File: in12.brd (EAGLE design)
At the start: 146.1 x 43.2 mm, 34 parts, among them U1 MICROCHIP_HV5622PG-GMICROCHIP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, U2 MICROCHIP_HV5622PG-GMICROCHIP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, U3 MICROCHIP_HV5622PG-GMICROCHIP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

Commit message: 5523 still need shuffle pins
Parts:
- removed U1, U2, U3: MICROCHIP_HV5622PG-GMICROCHIP_HV5622PG-G_0_0, Microchip - HV5622PG-G:MICROCHIP_HV5622PG-G_0
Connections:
- net L10: no longer U1.35
- net L11: no longer U1.40
- net L12: no longer U1.44
- net L13: no longer U1.43
- net L14: no longer U1.42
- net L15: no longer U1.41
- net L16: no longer U1.39
- net L17: no longer U1.37
- net L18: no longer U1.36
- net L19: no longer U1.38
- net L1D: no longer U1.1
- net L20: no longer U1.2
- net L21: no longer U1.7
- net L22: no longer U1.11
- net L23: no longer U1.10
- net L24: no longer U1.9
- net L25: no longer U1.8
- net L26: no longer U1.6
- net L27: no longer U1.4
- net L28: no longer U1.3
- net L29: no longer U1.5
- net L2D: no longer U1.22
- net L30: no longer U1.12
- net L31: no longer U1.17
- net L32: no longer U1.21
- net L33: no longer U1.20
- net L34: no longer U1.19
- net L35: no longer U1.18
- net L36: no longer U1.16
- net L37: no longer U1.14
- net L38: no longer U1.13
- net L39: no longer U1.15
- net L3D: now also U5.35; no longer U2.35
- net L40: now also U5.36; no longer U2.36
- net L41: now also U5.41; no longer U2.41
- net L42: now also U5.4; no longer U2.4
- net L43: now also U5.2; no longer U2.2
- net L44: now also U5.43; no longer U2.43
- net L45: now also U5.42; no longer U2.42
- net L46: now also U5.40; no longer U2.40
- net L47: now also U5.38; no longer U2.38
- net L48: now also U5.37; no longer U2.37
- net L49: now also U5.39; no longer U2.39
- net L4D: now also U5.5; no longer U2.5
- net L50: now also U5.7; no longer U2.7
- net L51: now also U5.13; no longer U2.13
- net L52: now also U5.17; no longer U2.17
- net L53: now also U5.16; no longer U2.16
- net L54: now also U5.15; no longer U2.15
- net L55: now also U5.14; no longer U2.14
- net L56: now also U5.12; no longer U2.12
- net L57: now also U5.10; no longer U2.10
- net L58: now also U5.8; no longer U2.8
- net L59: now also U5.11; no longer U2.11
- net L5D: now also U5.18; no longer U2.18
- net L60: now also U5.19; no longer U2.19
- net L61: now also U6.36; no longer U3.36
- net L62: now also U6.43; no longer U3.43
- net L63: now also U6.42; no longer U3.42
- net L64: now also U6.38; no longer U3.38
- net L65: now also U6.37; no longer U3.37
- net L66: now also U6.35; no longer U3.35
- net L67: now also U5.22; no longer U2.22
- net L68: now also U5.21; no longer U2.21
- net L69: now also U5.20; no longer U2.20
- net L6D: now also U6.44; no longer U3.44
- net L70: now also U6.1; no longer U3.1
- net L71: now also U6.6; no longer U3.6
- net L72: now also U6.10; no longer U3.10
- net L73: now also U6.9; no longer U3.9
- net L74: now also U6.8; no longer U3.8
- net L75: now also U6.7; no longer U3.7
- net L76: now also U6.5; no longer U3.5
- net L77: now also U6.3; no longer U3.3
- net L78: now also U6.2; no longer U3.2
- net L79: now also U6.4; no longer U3.4
- net L7D: now also U6.11; no longer U3.11
- net L80: now also U6.12; no longer U3.12
- net L81: now also U6.17; no longer U3.17
- net L82: now also U6.21; no longer U3.21
- net L83: now also U6.20; no longer U3.20
- net L84: now also U6.19; no longer U3.19
- net L85: now also U6.18; no longer U3.18
- net L86: now also U6.16; no longer U3.16
- net L87: now also U6.14; no longer U3.14
- net L88: now also U6.13; no longer U3.13
- net L89: now also U6.15; no longer U3.15
- net L8D: now also U6.22; no longer U3.22
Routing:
- net L10: track 57.2 -> 13.2 mm
- net L8D: track 72.8 -> 30.7 mm
- net L82: track 58.2 -> 17.1 mm
- net L83: track 50.4 -> 10.8 mm
- net L18: track 43.3 -> 4.93 mm
- net L84: track 43.0 -> 6.01 mm
- net L17: track 36.9 -> 2.40 mm
- net L85: track 37.5 -> 3.11 mm
- net L81: track 51.6 -> 20.0 mm
- net L19: track 42.8 -> 12.2 mm
- net L86: track 31.0 -> 2.74 mm
- net L16: track 29.6 -> 2.93 mm
- net L51: track 26.5 -> 0.00 mm
- net L89: track 39.4 -> 13.0 mm
- net L3D: track 39.0 -> 14.3 mm
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
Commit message: hv single layer routed
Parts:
- added U$1: DS3232, ds3232:SO20-2
- moved R1 9.58 mm to (2.29, 8.00), turned to 270 degrees
- moved R16 9.27 mm to (144.1, 8.64), turned to 90 degrees
- moved R7 4.76 mm to (110.4, 7.75)
- moved R6 4.68 mm to (92.2, 7.37)
- moved R5 4.60 mm to (74.5, 7.37)
- moved R8 4.47 mm to (128.3, 7.49)
- moved R2 4.42 mm to (21.3, 7.24)
- moved R3 4.42 mm to (39.1, 7.24)
- moved R4 4.37 mm to (57.1, 7.37)
- moved U4 2.18 mm to (36.8, 30.0)
- moved U6 1.99 mm to (108.8, 30.0)
- moved U5 1.37 mm to (72.4, 30.0), turned to 135 degrees
- moved R9 1.25 mm to (17.9, 7.11)
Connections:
- net L2D: now also U4.12; no longer U4.22
- net L30: now also U4.13; no longer U4.12
- net L31: now also U4.18; no longer U4.17
- net L32: now also U4.22; no longer U4.21
- net L33: now also U4.21; no longer U4.20
- net L34: now also U4.20; no longer U4.19
- net L35: now also U4.19; no longer U4.18
- net L36: now also U4.17; no longer U4.16
- net L37: now also U4.15; no longer U4.14
- net L38: now also U4.14; no longer U4.13
- net L39: now also U4.16; no longer U4.15
- net L41: now also U5.42; no longer U5.41
- net L42: now also U5.1; no longer U5.4
- net L43: now also U5.44; no longer U5.2
- net L45: now also U5.41; no longer U5.42
- net L4D: now also U5.2; no longer U5.5
- net L50: now also U5.3; no longer U5.7
- net L51: now also U5.8; no longer U5.13
- net L52: now also U5.12; no longer U5.17
- net L53: now also U5.11; no longer U5.16
- net L54: now also U5.10; no longer U5.15
- net L55: now also U5.9; no longer U5.14
- net L56: now also U5.7; no longer U5.12
- net L57: now also U5.5; no longer U5.10
- net L58: now also U5.4; no longer U5.8
- net L59: now also U5.6; no longer U5.11
- net L5D: now also U5.13; no longer U5.18
- net L60: now also U5.14; no longer U5.19
- net L61: now also U6.39; no longer U6.36
- net L64: now also U6.41; no longer U6.38
- net L65: now also U6.40; no longer U6.37
- net L66: now also U6.38; no longer U6.35
- net L67: now also U6.37; no longer U5.22
- net L68: now also U6.36; no longer U5.21
- net L69: now also U6.35; no longer U5.20
- net L71: now also U6.5; no longer U6.6
- net L76: now also U6.6; no longer U6.5
- net L77: now also U6.4; no longer U6.3
- net L79: now also U6.3; no longer U6.4
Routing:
- net HV: track 119.3 -> 0.00 mm
- net VDD: track 0.00 -> 77.7 mm
- net L10: track 13.2 -> 52.1 mm
- net L82: track 17.1 -> 53.9 mm
- net L83: track 10.8 -> 47.0 mm
- net L18: track 4.93 -> 40.6 mm
- net L84: track 6.01 -> 39.8 mm
- net L17: track 2.40 -> 34.2 mm
- net L85: track 3.11 -> 34.5 mm
- net L19: track 12.2 -> 41.1 mm
- net L81: track 20.0 -> 48.7 mm
- net L51: track 0.00 -> 27.3 mm
- net L86: track 2.74 -> 28.3 mm
- net L8D: track 30.7 -> 55.7 mm
- net L16: track 2.93 -> 27.7 mm
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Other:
- board size 146.1 x 43.2 mm -> 146.1 x 38.1 mm

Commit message: compact
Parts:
- added IC1: LM1117MPX-3.3_NOPB, SamacSys_Parts:SOT230P700X180-4N
- added U$2: HV_PSU, SamacSys_Parts:HV_PSU
- added U1: ESP32-WROOM-32D, SamacSys_Parts:MODULE_ESP32-WROOM-32D
- moved R16 9.67 mm to (134.5, 8.13), turned to 0 degrees
- moved SV1 9.67 mm to (12.2, 56.6)
- moved R13 8.65 mm to (81.5, 8.13), turned to 0 degrees
- moved R10 8.64 mm to (28.2, 8.00), turned to 0 degrees
- moved R14 8.52 mm to (99.4, 8.13), turned to 0 degrees
- moved R11 8.52 mm to (46.1, 8.00), turned to 0 degrees
- moved R12 8.52 mm to (63.9, 8.00), turned to 0 degrees
- moved R15 8.51 mm to (117.2, 7.75), turned to 0 degrees
- moved R9 7.42 mm to (10.5, 8.00), turned to 0 degrees
- moved R1 4.19 mm to (2.41, 3.81)
- moved R7 4.14 mm to (109.1, 3.81)
- moved R8 3.94 mm to (126.9, 3.81)
- moved R4 3.82 mm to (55.8, 3.81)
- moved R5 3.70 mm to (73.5, 3.81)
- moved R6 3.67 mm to (91.3, 3.81)
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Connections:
- new net 3V3: U1.2
- new net GND: U1.1, U1.15, U1.38, U1.39_1, U1.39_10, U1.39_11, U1.39_12, U1.39_13, U1.39_14, U1.39_15, U1.39_16, U1.39_17, U1.39_18, U1.39_19, U1.39_2, U1.39_20, U1.39_21, U1.39_3, U1.39_4, U1.39_5, U1.39_6, U1.39_7, U1.39_8, U1.39_9
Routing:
- net HV: track 0.00 -> 144.4 mm
- net L8D: track 55.7 -> 68.7 mm
- net L2D: track 17.5 -> 29.3 mm
- net L5D: track 34.8 -> 46.5 mm
- net L6D: track 17.6 -> 29.1 mm
- net L3D: track 33.9 -> 45.1 mm
- net L4D: track 18.6 -> 29.9 mm
- net L1D: track 32.4 -> 42.8 mm
- net L7D: track 33.2 -> 42.5 mm
- net N$15: track 10.0 -> 3.98 mm
- net N$11: track 10.0 -> 4.23 mm
- net N$12: track 10.0 -> 4.23 mm
- net N$10: track 10.0 -> 4.28 mm
- net N$14: track 10.0 -> 4.36 mm
- net N$13: track 10.0 -> 4.41 mm
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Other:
- board size 146.1 x 38.1 mm -> 146.1 x 33.7 mm

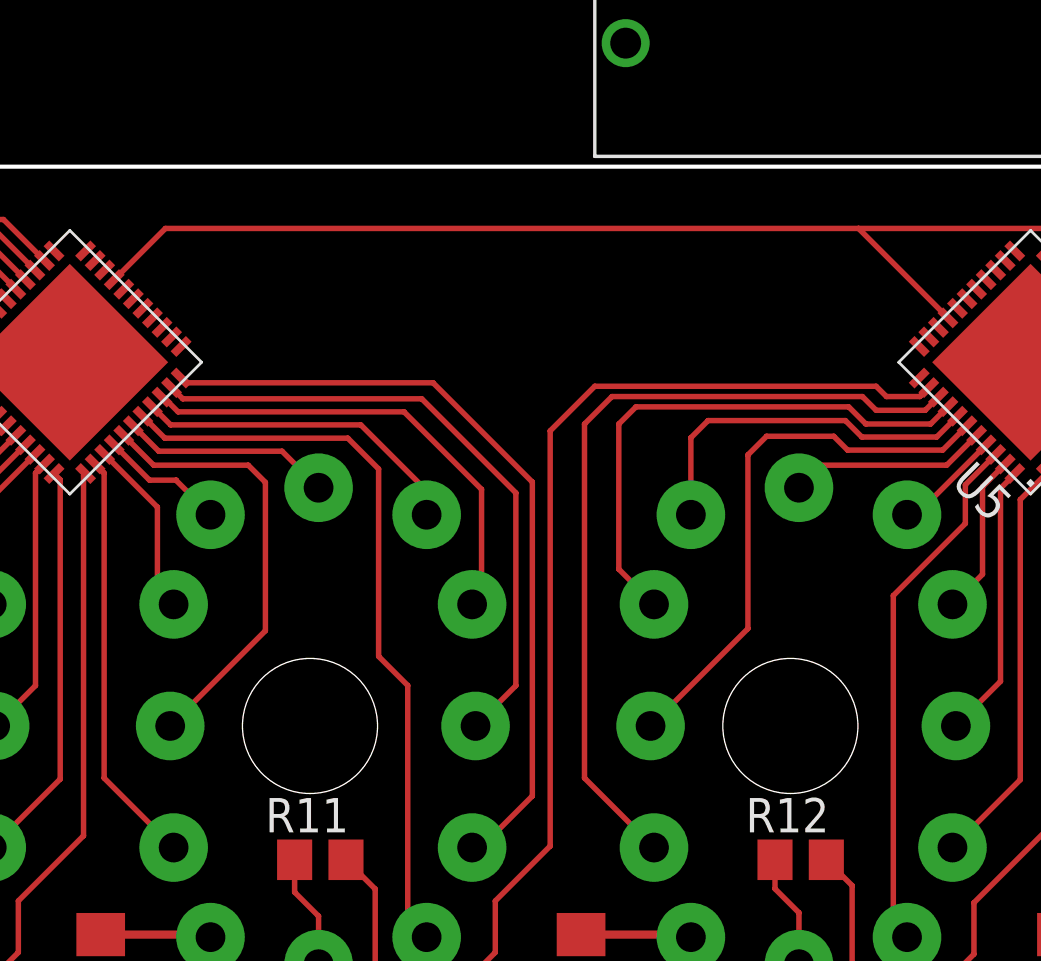
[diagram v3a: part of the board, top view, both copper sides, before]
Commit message: added m.2 connector
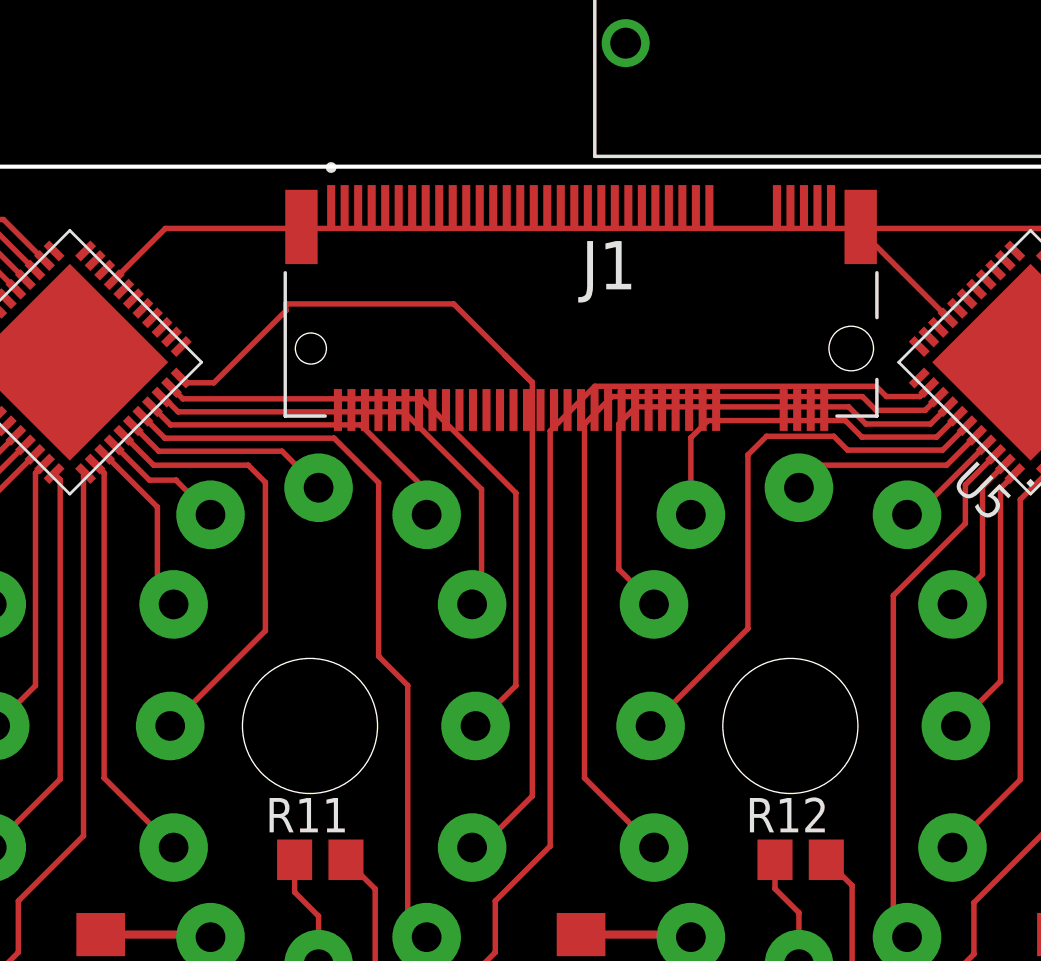
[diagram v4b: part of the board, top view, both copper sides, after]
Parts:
- added J1: 1-2199230-6, 1-2199230-6:TE_1-2199230-6
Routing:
- net L32: track 29.2 -> 35.4 mm
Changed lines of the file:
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@@
 <param name="mdViaViaSameLayer" value="6mil"/>
 <param name="mnLayersViaInSmd" value="2"/>
-<param name="mdCopperDimension" value="40mil"/>
+<param name="mdCopperDimension" value="20mil"/>
 <param name="mdDrill" value="6mil"/>
 <param name="mdSmdStop" value="0mil"/>
@@
 <attribute name="VALUE" x="-29.21" y="6.223" size="1.27" layer="27" align="center"/>
 </element>
+<element name="J1" library="1-2199230-6" package="TE_1-2199230-6" value="1-2199230-6" x="55.753" y="26.924" smashed="yes">
+<attribute name="AVAILABILITY" value="In Stock" x="55.753" y="26.924" size="1.778" layer="27" display="off"/>
+<attribute name="CENTERLINE_PITCH" value=".5 mm[.0197 in]" x="55.753" y="26.924" size="1.778" layer="27" display="off"/>
+<attribute name="CHECK_PRICES" value="https://www.snapeda.com/parts/1-2199230-6/TE+Connectivity+AMP+Connectors/view-part/?ref=eda" x="55.753" y="26.924" size="1.778" layer="27" display="off"/>
+<attribute name="COMMENT" value="1-2199230-6" x="55.753" y="26.924" size="1.778" layer="27" display="off"/>
+<attribute name="DESCRIPTION" value=" 67 Position Female Connector M.2 (NGFF) Mini Card Gold 0.020 (0.50mm) Black " x="55.753" y="26.924" size="1.778" layer="27" display="off"/>
+<attribute name="MF" value="TE Connectivity" x="55.753" y="26.924" size="1.778" layer="27" display="off"/>
+<attribute name="MP" value="1-2199230-6" x="55.753" y="26.924" size="1.778" layer="27" display="off"/>
+<attribute name="NAME" x="55.762" y="29.1151" size="1.78473125" layer="25"/>
+<attribute name="NUMBER_OF_POSITIONS" value="67" x="55.753" y="26.924" size="1.778" layer="27" display="off"/>
+<attribute name="PACKAGE" value="None" x="55.753" y="26.924" size="1.778" layer="27" display="off"/>
+<attribute name="PRICE" value="None" x="55.753" y="26.924" size="1.778" layer="27" display="off"/>
+<attribute name="PRODUCT_TYPE" value="Socket" x="55.753" y="26.924" size="1.778" layer="27" display="off"/>
+<attribute name="PURCHASE-URL" value="https://www.snapeda.com/api/url_track_click_mouser/?unipart_id=587628&amp;manufacturer=TE Connectivity&amp;part_name=1-2199230-6&amp;search_term=m.2 " x="55.753" y="26.924" size="1.778" layer="27" display="off"/>
+<attribute name="SNAPEDA_LINK" value="https://www.snapeda.com/parts/1-2199230-6/TE+Connectivity+AMP+Connectors/view-part/?ref=snap" x="55.753" y="26.924" size="1.778" layer="27" display="off"/>
+<attribute name="VALUE" x="49.2609" y="26.84705" size="1.78876875" layer="27"/>
+</element>
 </elements>
 <signals>
@@
 <wire x1="50.0375" y1="5.1365" x2="49.3376" y2="5.8364" width="0.2032" layer="1"/>
 <wire x1="49.3376" y1="5.8364" x2="49.3376" y2="14.4524625" width="0.2032" layer="1"/>
-<wire x1="48.26" y1="15.5300625" x2="48.26" y2="22.4662625" width="0.2032" layer="1"/>
+<wire x1="48.26" y1="15.5300625" x2="48.26" y2="21.9582625" width="0.2032" layer="1"/>
 <contactref element="U4" pad="18"/>
 <wire x1="39.53468125" y1="24.418421875" x2="40.347521875" y2="23.605584375" width="0.2032" layer="1"/>
-<wire x1="40.347521875" y1="23.605584375" x2="47.120678125" y2="23.605584375" width="0.2032" layer="1"/>
-<wire x1="47.120678125" y1="23.605584375" x2="48.26" y2="22.4662625" width="0.2032" layer="1"/>
+<wire x1="40.347521875" y1="23.605584375" x2="46.612678125" y2="23.605584375" width="0.2032" layer="1"/>
+<wire x1="46.612678125" y1="23.605584375" x2="48.26" y2="21.9582625" width="0.2032" layer="1"/>
 </signal>
 <signal name="L32">
@@
 <wire x1="53.9496" y1="10.3613375" x2="52.0422625" y2="8.454" width="0.2032" layer="1"/>
 <wire x1="51.72" y1="8.454" x2="52.0422625" y2="8.454" width="0.2032" layer="1"/>
-<wire x1="53.9496" y1="10.3613375" x2="53.9496" y2="21.981125" width="0.2032" layer="1"/>
+<wire x1="53.9496" y1="10.3613375" x2="53.9496" y2="25.664125" width="0.2032" layer="1"/>
 <contactref element="U4" pad="22"/>
-<wire x1="50.274865625" y1="25.655859375" x2="41.125671875" y2="25.655859375" width="0.2032" layer="1"/>
+<wire x1="41.125671875" y1="25.655859375" x2="42.164" y2="25.655859375" width="0.2032" layer="1"/>
 <wire x1="40.948896875" y1="25.832634375" x2="41.125671875" y2="25.655859375" width="0.2032" layer="1"/>
-<wire x1="50.274865625" y1="25.655859375" x2="53.9496" y2="21.981125" width="0.2032" layer="1"/>
+<wire x1="52.941865625" y1="26.671859375" x2="52.943725" y2="26.67" width="0.2032" layer="1"/>
+<wire x1="52.943725" y1="26.67" x2="53.9496" y2="25.664125" width="0.2032" layer="1"/>
+<wire x1="42.164" y1="25.655859375" x2="44.831" y2="28.322859375" width="0.2032" layer="1"/>
+<wire x1="44.831" y1="28.322859375" x2="44.831" y2="28.575" width="0.2032" layer="1"/>
+<wire x1="44.831" y1="28.575" x2="51.038725" y2="28.575" width="0.2032" layer="1"/>
+<wire x1="51.038725" y1="28.575" x2="53.935725" y2="25.678" width="0.2032" layer="1"/>
+<wire x1="53.935725" y1="25.678" x2="53.9496" y2="25.678" width="0.2032" layer="1"/>
+<wire x1="52.941865625" y1="26.671859375" x2="53.9496" y2="25.678" width="0" layer="19" extent="1-1"/>
 </signal>
 <signal name="L33">

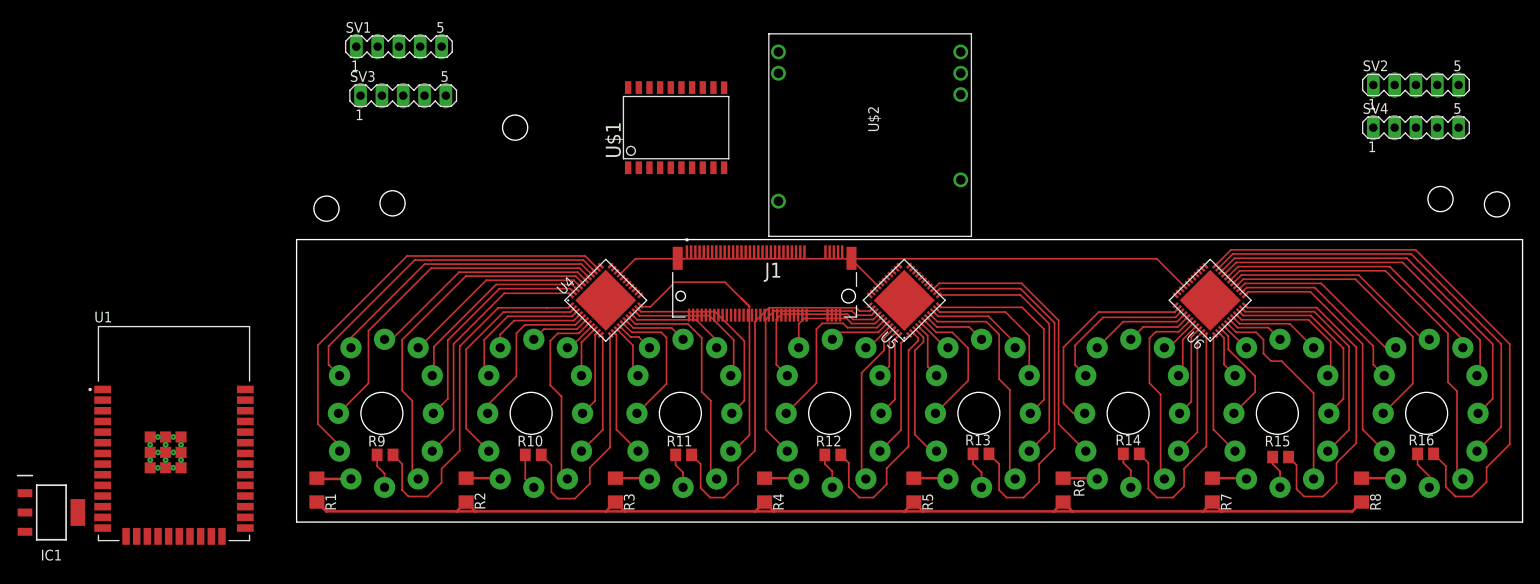
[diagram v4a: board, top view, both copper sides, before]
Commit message: control board, adapter ffc wire
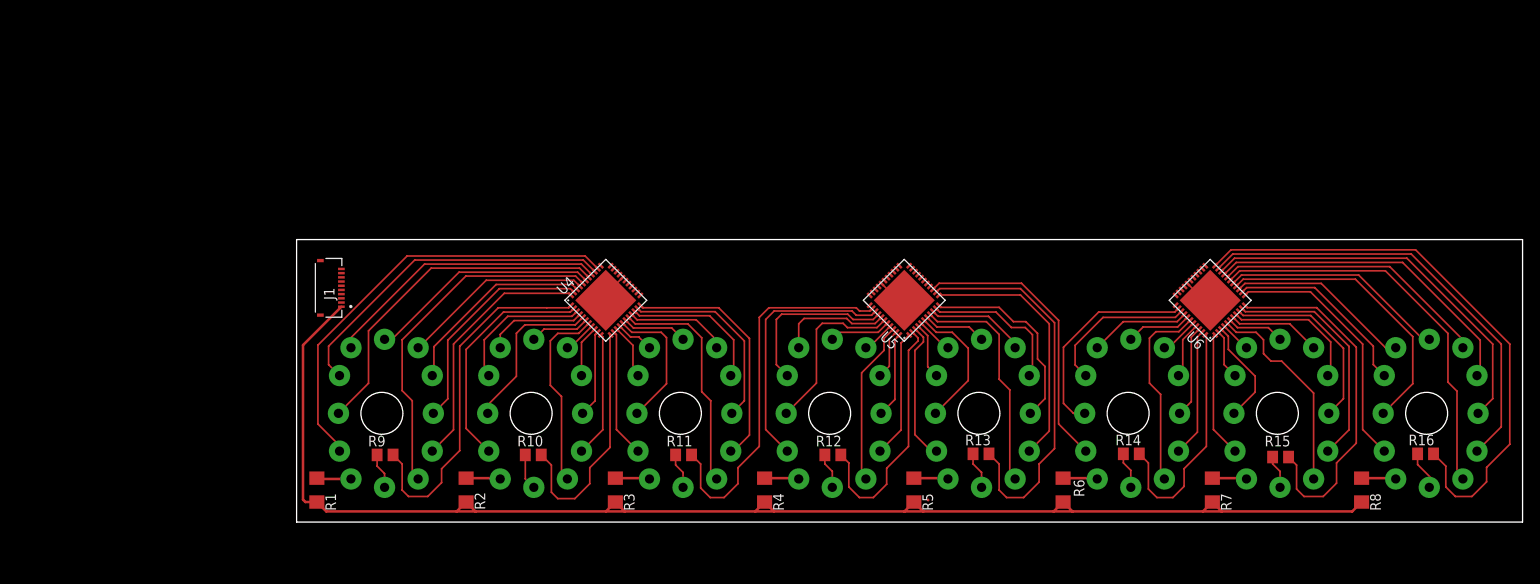
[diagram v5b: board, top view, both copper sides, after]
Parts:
- removed IC1: LM1117MPX-3.3_NOPB, SamacSys_Parts:SOT230P700X180-4N
- removed SV1, SV2, SV3, SV4: (no value), con-lstb:MA05-1
- removed U$1: DS3232, ds3232:SO20-2
- removed U$2: HV_PSU, SamacSys_Parts:HV_PSU
- removed U1: ESP32-WROOM-32D, SamacSys_Parts:MODULE_ESP32-WROOM-32D
- J1: value 1-2199230-6 -> 1-2328702-0; device 1-2199230-6:TE_1-2199230-6 -> 1-2328702-0:TE_1-2328702-0
- moved J1 50.4 mm to (5.33, 25.7), turned to 270 degrees
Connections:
- removed net EXP: U4.EXP, U5.EXP, U6.EXP
- removed net VDD: U4.30, U5.30, U6.30
- removed net VSS: U4.29, U5.29, U6.29
- new net BL: J1.9, U4.33, U5.33, U6.33
- new net CLK: J1.4, U4.28, U5.28, U6.28
- new net IN: J1.8, U4.32
- new net LE: J1.7, U4.31, U5.31, U6.31
- new net N$17: U4.23, U5.32
- new net N$18: U5.23, U6.32
- new net OUT: J1.10, U6.23
- new net POL: J1.3, U4.27, U5.27, U6.27
- net 3V3: now also J1.6, U4.30, U5.30, U6.30; no longer U1.2
- net GND: now also J1.5, U4.29, U4.EXP, U5.29, U5.EXP, U6.29, U6.EXP; no longer U1.1, U1.15, U1.38, U1.39_1, U1.39_10, U1.39_11, U1.39_12, U1.39_13, U1.39_14, U1.39_15, U1.39_16, U1.39_17, U1.39_18, U1.39_19, U1.39_2, U1.39_20, U1.39_21, U1.39_3, U1.39_4, U1.39_5, U1.39_6, U1.39_7, U1.39_8, U1.39_9
- net HV: now also J1.1
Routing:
- net VDD: track 74.1 -> 0.00 mm
- net HV: track 144.4 -> 171.1 mm
- net GND: track 0.00 -> 10.6 mm
- net L32: track 35.4 -> 29.2 mm
- net L53: track 24.4 -> 23.8 mm
- net L54: track 17.2 -> 17.8 mm
